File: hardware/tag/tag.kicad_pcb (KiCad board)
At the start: 2 copper layers, 50 x 52 mm, 118 parts, among them J1 USB_C_Receptacle_USB2.0_16P, J10 Conn_01x02, J2 BATTERY, J3 BLE_Conn, J4 SOURCE, J5 STM SWD, J6 I2C, J7 UART, J8 BLE SWD, J9 I2C, Q1 AO664, SW1 PWR, SW2 RESET, SW3 USER, U1 MAX17048G_T10, U2 USBLC6-2SC6, U3 ICM-45686, U4 TPS63070RNMR, U5 BQ24075RGT, U6 FSC-BT630, U7 STM32F411CEUx, U8 DWM1000, Y1 NX3215SA-32.768kHz(DNP), Y2 NX3225SA-24MHz

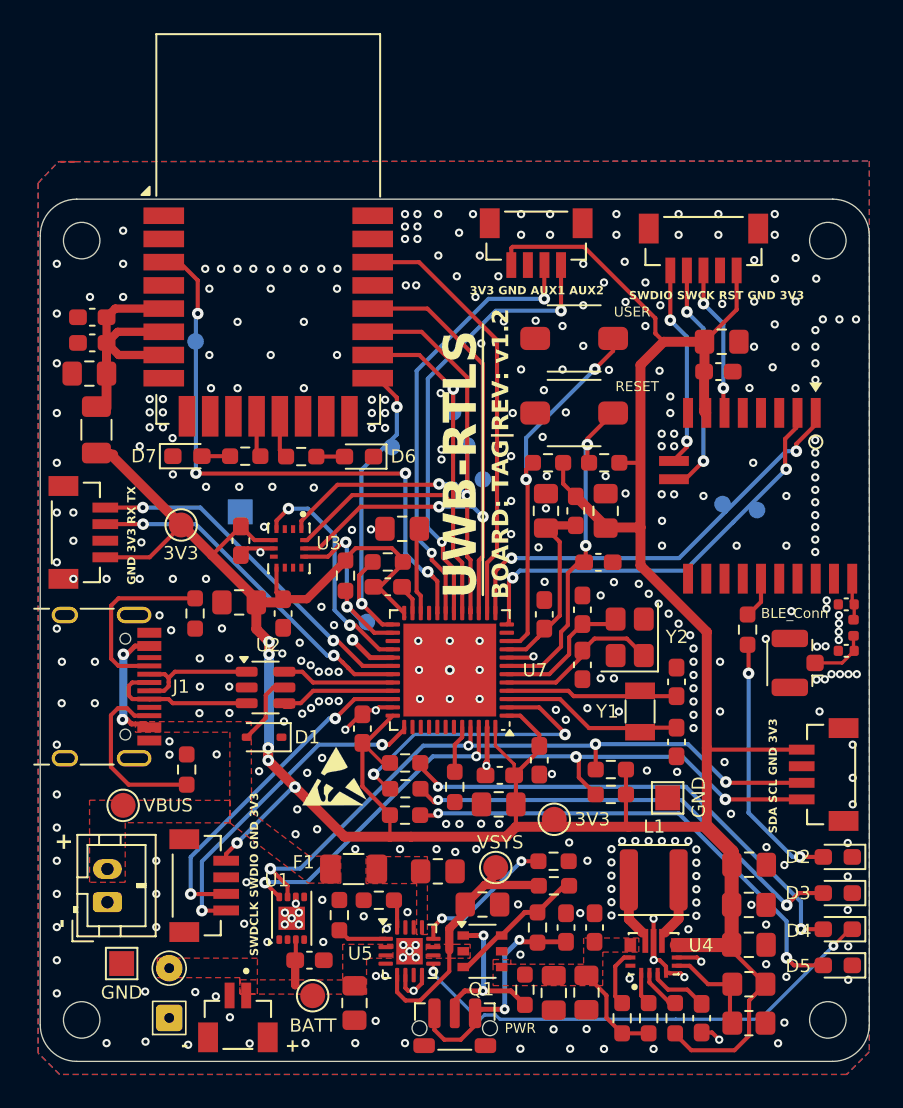
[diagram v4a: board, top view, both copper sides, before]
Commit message: update(hw): add schottky diode to prevent reverse current between USB and 5V header
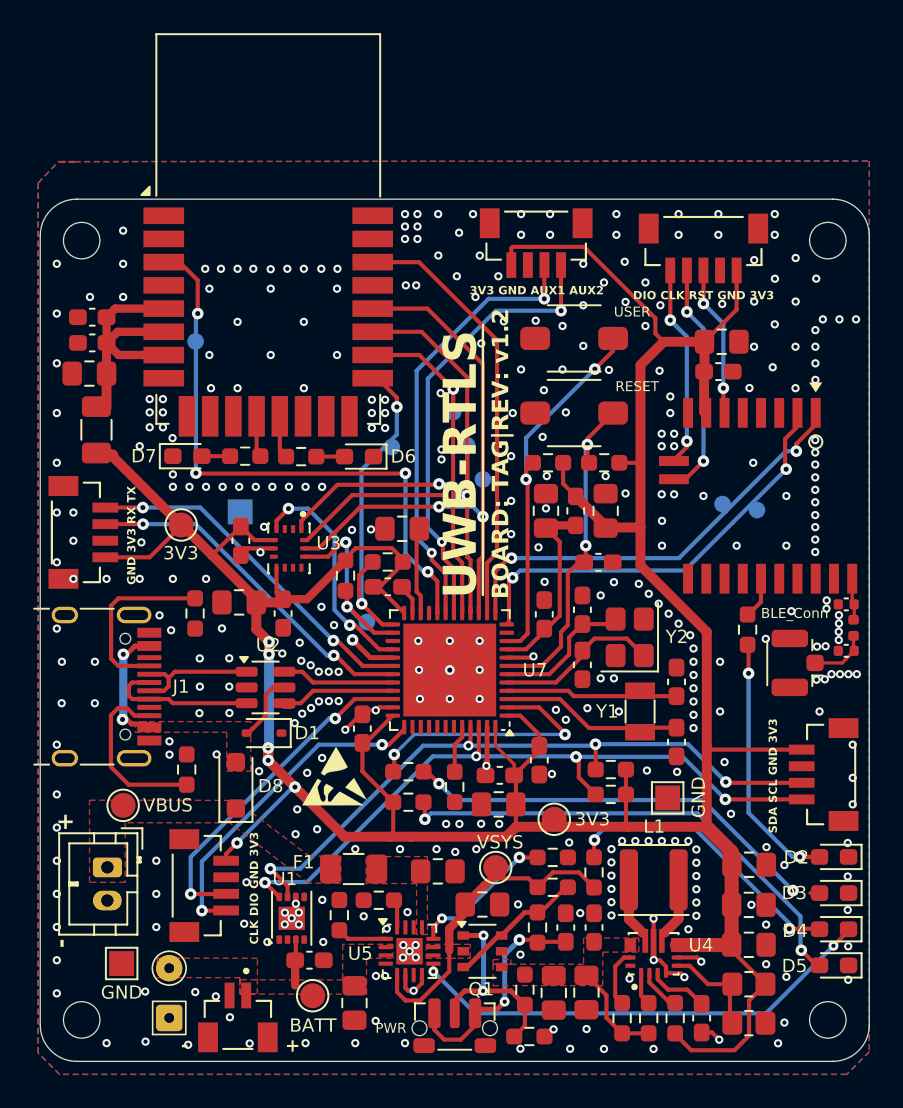
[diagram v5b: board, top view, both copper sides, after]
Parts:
- added D8: D_Schottky, Diode_SMD:D_SOD-123F, F.Cu at (42.8, 85.5)
- added R27: 470K, Resistor_SMD:R_0603_1608Metric_Pad0.98x0.95mm_HandSolder, F.Cu at (60.5, 100.6)
- R14: value 10k -> 470K
- moved R19 13.2 mm to (64.4, 90.7), turned to -90 degrees
- moved J4 2.10 mm to (35.0, 90.4), turned to -90 degrees
- moved R18 1.05 mm to (53.2, 84.6)
- moved R20 0.81 mm to (53.2, 86.5)
- moved D1 0.25 mm to (44.5, 82.3)
- moved R5 0.23 mm to (61.9, 89.8)
- moved D2 0.22 mm to (78.9, 89.8)
- moved D3 0.22 mm to (78.9, 92.0)
- moved D4 0.22 mm to (78.9, 94.1)
- moved D5 0.22 mm to (78.9, 96.3)
- moved R13 0.11 mm to (61.9, 91.6)
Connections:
- D1 pad 2: VBUS -> /V_USB
- J1 pad A4: VBUS -> /V_USB
- J1 pad A9: VBUS -> /V_USB
- J1 pad B4: VBUS -> /V_USB
- J1 pad B9: VBUS -> /V_USB
- J4 pad 1: GND -> VBUS
- J4 pad 2: VBUS -> GND
- R19 pad 2: +3.3V -> /SYS
- U2 pad 5: VBUS -> /V_USB
- U7 pad 38: unconnected-(U7-PA15-Pad38) -> /LED_PM
- U7 pad 39: /CHANGER SENSE -> unconnected-(U7-PB3-Pad39)
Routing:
- net VBUS: track 12.0 -> 0.00 mm, vias 2 -> 0
- net /V_USB: track 0.00 -> 11.9 mm, vias 0 -> 2
- net Net-(D4-A): track 29.7 -> 17.9 mm
- net /SYS: track 15.6 -> 20.1 mm
- net Net-(Q1A-G1): track 10.3 -> 12.5 mm
- net /LED_USR: track 18.1 -> 16.1 mm
- net +3.3V: track 209.3 -> 207.3 mm
- net Net-(D3-A): track 27.6 -> 25.8 mm
- net Net-(D5-A): track 29.5 -> 30.4 mm
- net GND: vias 370 -> 375
- added copper zone on F.Cu, net /V_USB
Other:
- board text added: "${REFERENCE}"
- board text added: "CLK DIO GND 3V3"
- board text added: "DIO CLK RST GND 3V3"
- board text removed: "SWDCLK SWDIO GND 3V3"
- board text removed: "SWDIO SWCK RST GND 3V3"

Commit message: update: Add Python protobuf generation for vv_testings in Makefile
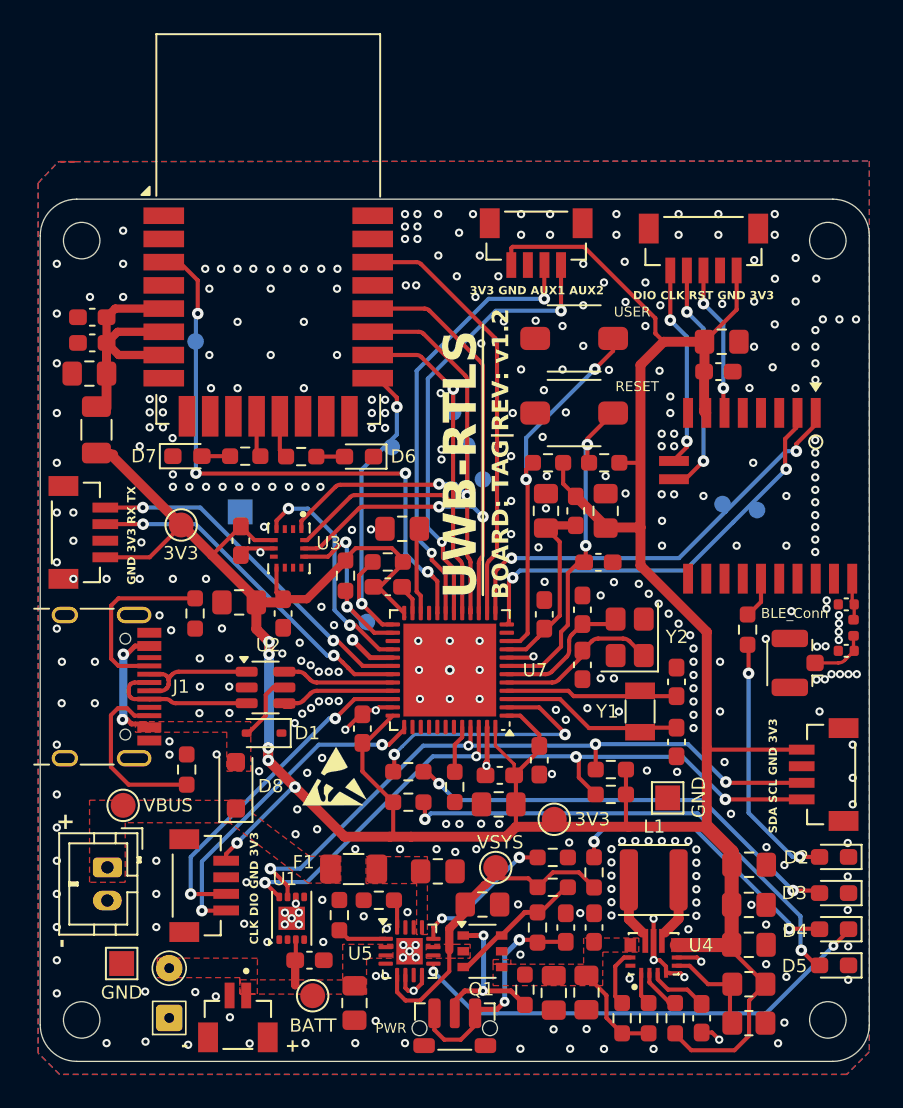
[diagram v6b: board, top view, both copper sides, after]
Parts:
- removed R27: 470K, Resistor_SMD:R_0603_1608Metric_Pad0.98x0.95mm_HandSolder
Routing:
- net Net-(Q1A-G1): track 12.5 -> 10.3 mm
- net Net-(D3-A): track 25.8 -> 26.9 mm
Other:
- board text removed: "${REFERENCE}"

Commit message: wip
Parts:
- moved F1 3.91 mm to (46.4, 88.8), turned to -40 degrees
- moved J4 1.05 mm to (36.1, 90.5)
- moved J3 0.48 mm to (76.4, 78.5)
- moved C26 0.41 mm to (79.6, 77.7)
- moved L2 0.41 mm to (80.0, 76.4)
- moved C25 0.40 mm to (79.6, 74.9)
- moved R16 0.33 mm to (73.3, 76.1)
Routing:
- net GND: vias 375 -> 378
